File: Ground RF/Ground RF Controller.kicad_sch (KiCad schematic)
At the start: 32 parts, among them J3 USB_C_Receptacle_USB2.0_16P, U1 CP2102N-A02-GQFN28R, U4 NCP1117-3.3_SOT223

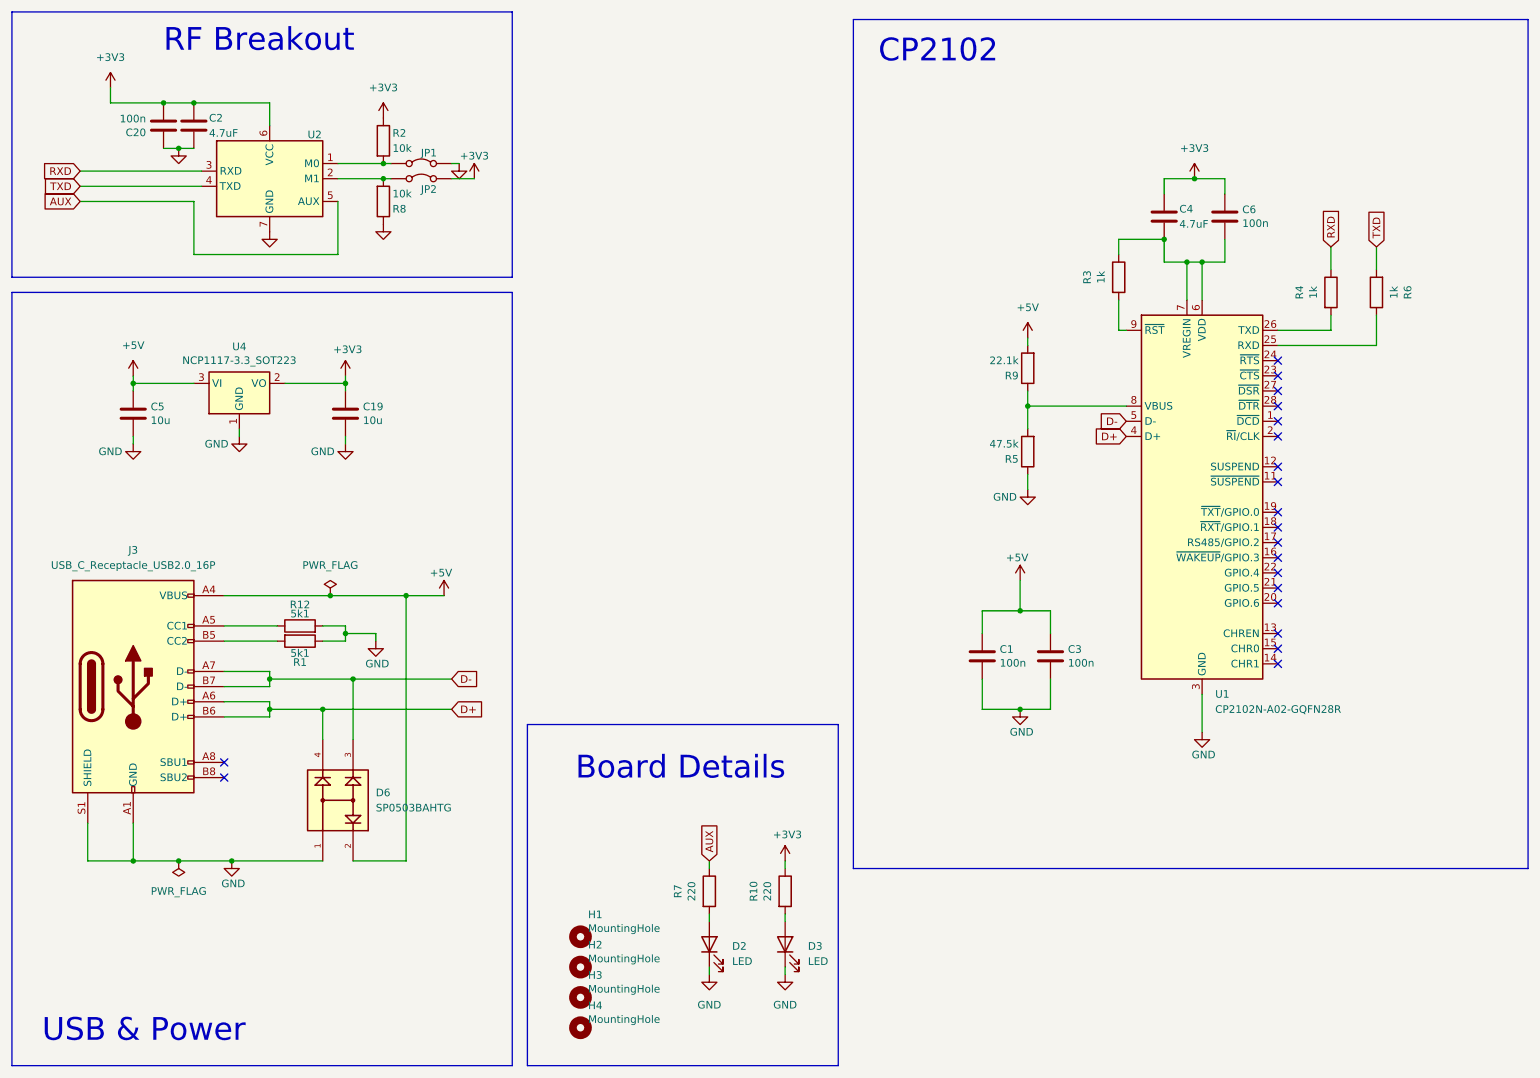
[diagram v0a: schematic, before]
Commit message: v2.0.0 Ground RF finished
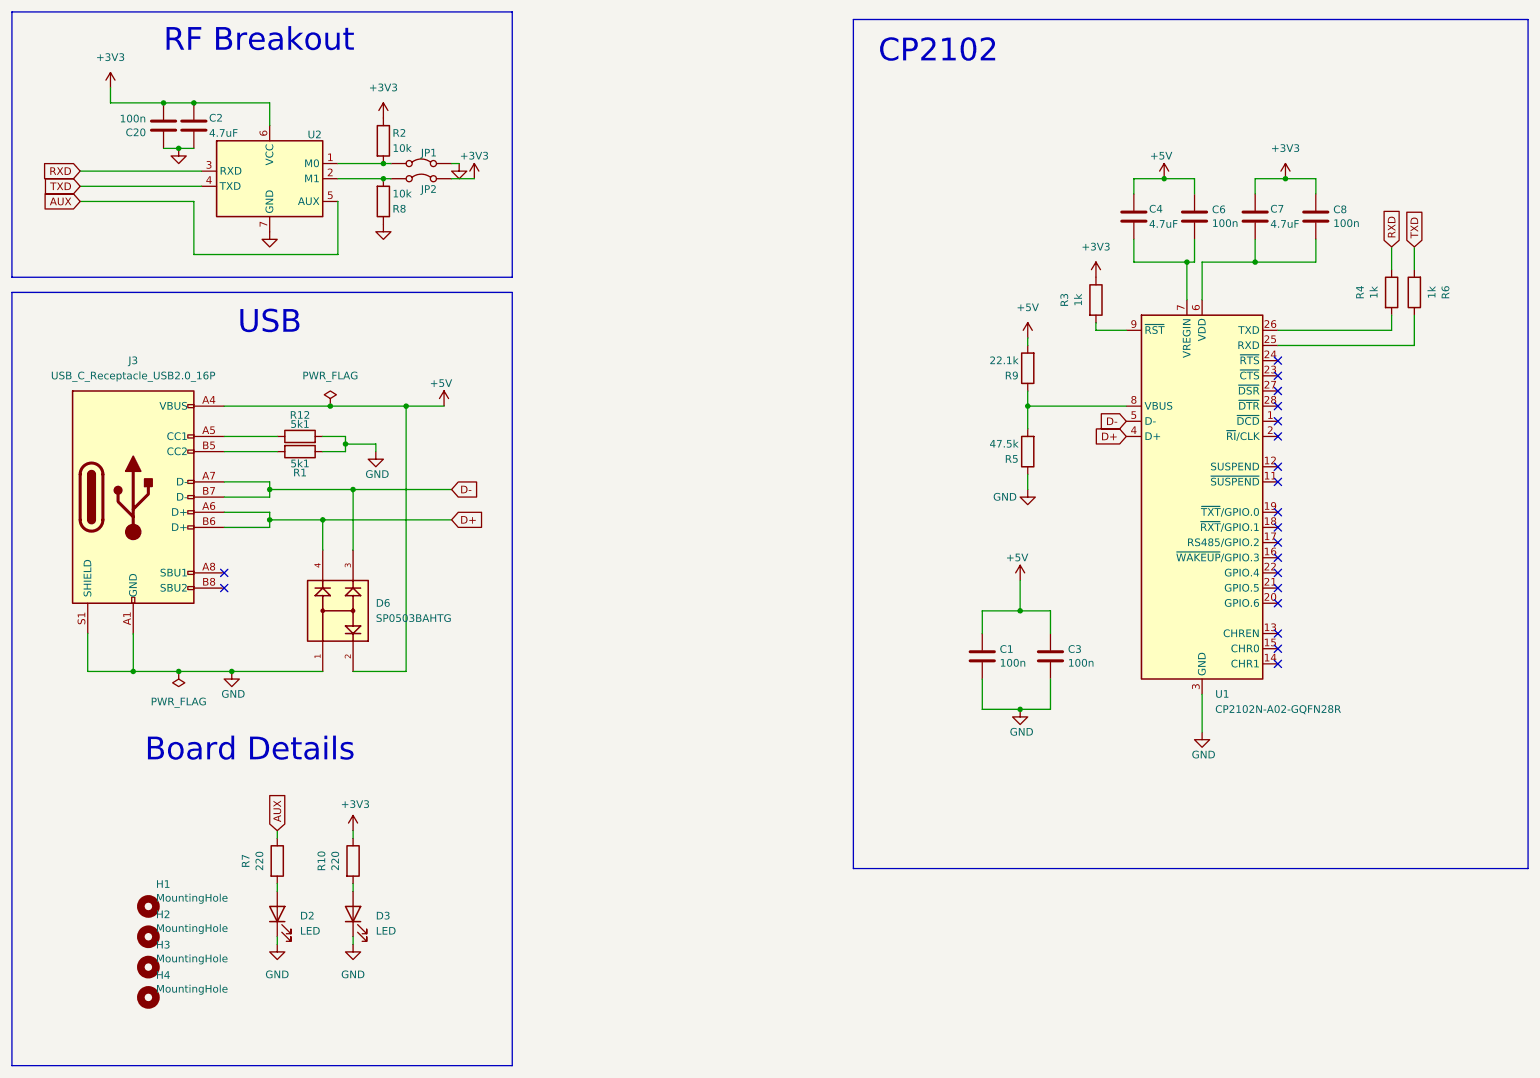
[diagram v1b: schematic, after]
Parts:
- removed C19, C5: 10u, Capacitor_SMD:C_1210_3225Metric, symbol Device:C
- removed U4: NCP1117-3.3_SOT223, Package_TO_SOT_SMD:SOT-223-3_TabPin2, symbol Regulator_Linear:NCP1117-3.3_SOT223
- added C7: 4.7uF, Capacitor_SMD:C_0402_1005Metric, symbol Device:C
- added C8: 100n, Capacitor_SMD:C_0402_1005Metric, symbol Device:C
- U2: footprint ottsky-rx:EBYTE-E220-900T22D -> Ground RF Controller:EBYTE-E220-900T22D
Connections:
- net +3V3: now also R3.1, C7.1, C8.1; no longer C4.1, C6.1
- net +5V: now also C4.1, C6.1
- net at C4.2, C6.2, U1.7 (VREGIN): no longer R3.1, U1.6 (VDD)
- new net: C7.2, C8.2, U1.6 (VDD)
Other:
- note added: "USB"
- note removed: "USB & Power"
- title: Ground RF Terminal -> Ground RF Controller
- moved on the sheet: C4, C6, D2, D3, D6, H1, H2, H3, H4, J3, R1, R10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
